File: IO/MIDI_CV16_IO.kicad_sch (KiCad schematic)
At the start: 111 parts, among them J1 Conn_01x10_Male, J10 AudioJack2_SwitchT, J11 Conn_01x10_Male, J12 AudioJack2_SwitchT, J13 AudioJack2_SwitchT, J14 AudioJack2_SwitchT, J15 AudioJack2_SwitchT, J16 AudioJack2_SwitchT, J17 AudioJack2_SwitchT, J18 AudioJack2_SwitchT, J19 AudioJack2_SwitchT, J2 Conn_01x10_Male, J20 Conn_01x10_Male, J3 AudioJack2_SwitchT, J4 AudioJack2_SwitchT, J5 AudioJack2_SwitchT, J6 AudioJack2_SwitchT, J7 AudioJack2_SwitchT, J8 AudioJack2_SwitchT, J9 AudioJack2_SwitchT, SW1 SW_SPST, SW2 SW_SPST, SW3 SW_SPST

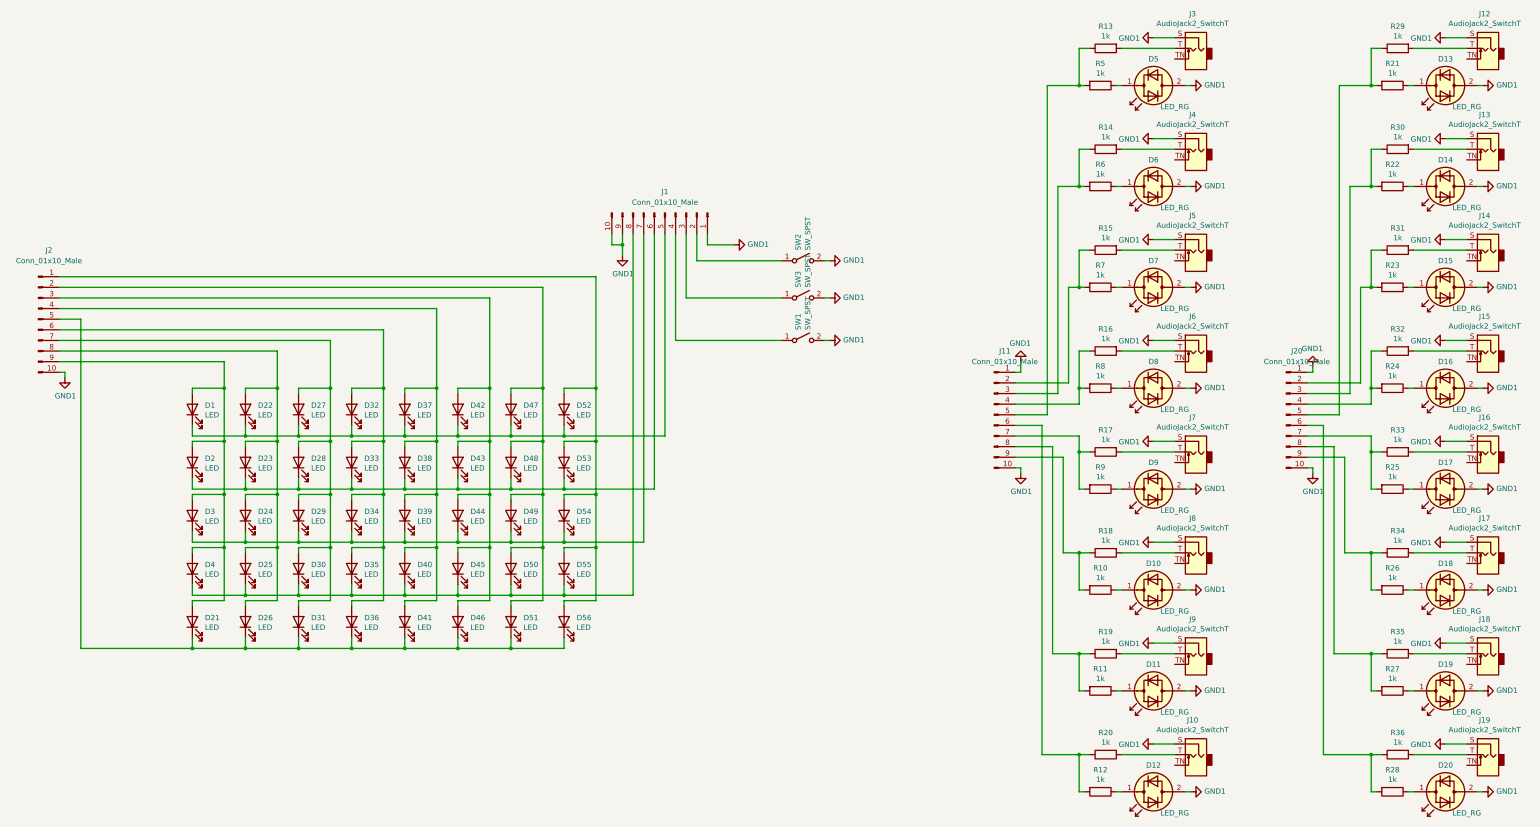
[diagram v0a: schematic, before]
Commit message: Update PCBs to V3.0
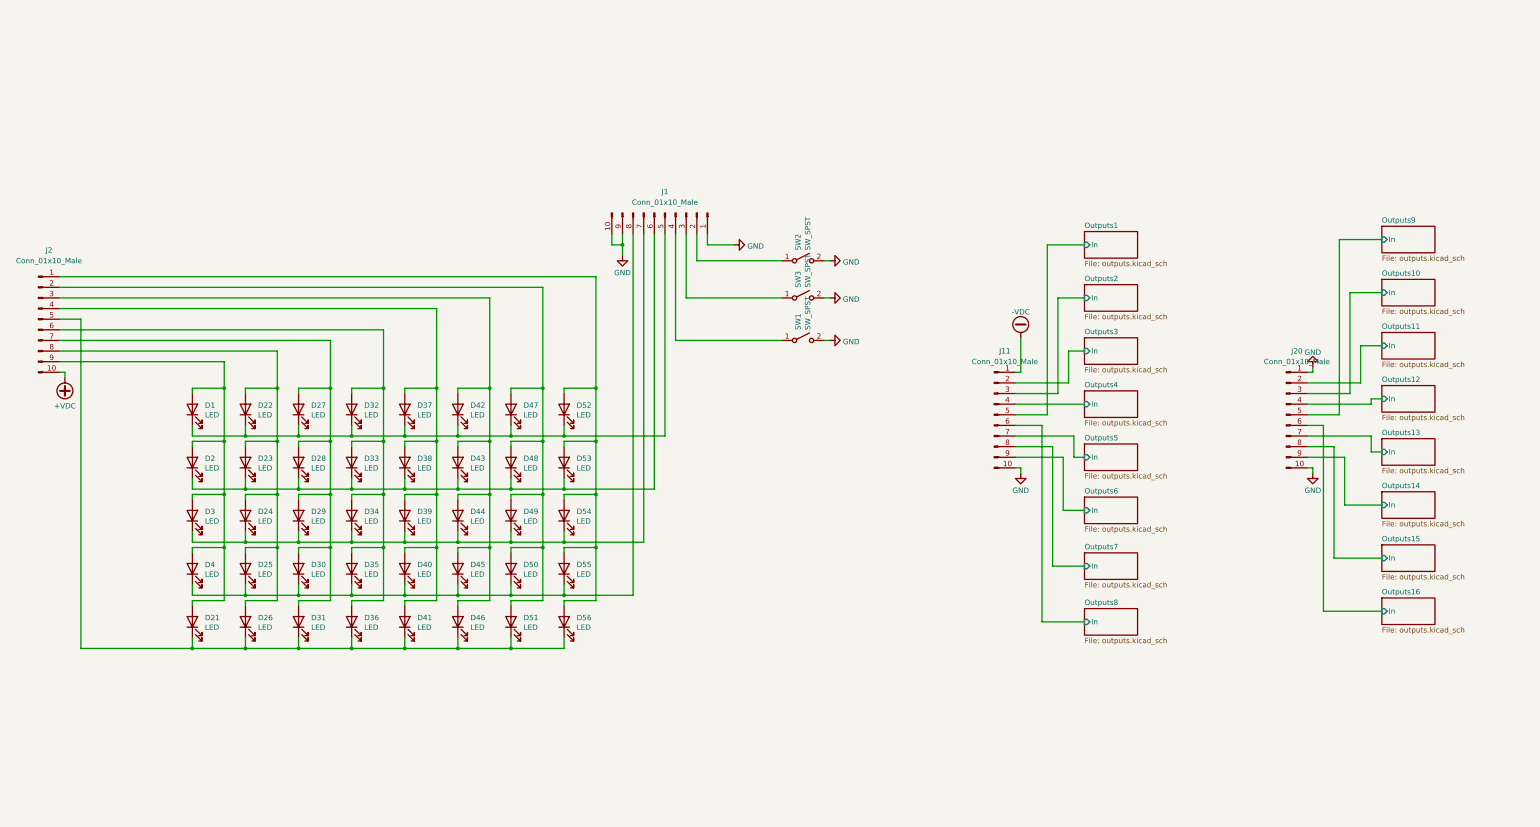
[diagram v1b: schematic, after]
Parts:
- removed D10, D11, D12, D13, D14, D15, D16, D17, D18, D19, D20, D5, D6, D7, D8, D9: LED_RG, LED_THT:LED_D5.0mm_FlatTop, symbol Device:LED_Dual_Bidirectional
- removed J10, J12, J13, J14, J15, J16, J17, J18, J19, J3, J4, J5, J6, J7, J8, J9: AudioJack2_SwitchT, Custom_FP:PJ398SM, symbol Connector_Audio:AudioJack2_SwitchT
- removed R10, R11, R12, R13, R14, R15, R16, R17, R18, R19, R20, R21, R22, R23, R24, R25, R26, R27, R28, R29, R30, R31, R32, R33, R34, R35, R36, R5, R6, R7, R8, R9: 1k, Resistor_SMD:R_0603_1608Metric, symbol Device:R
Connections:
- net Outputs3/In: now reaches J11.2 (Pin_2)
- net Outputs2/In: now reaches J11.3 (Pin_3)
- net Outputs4/In: now reaches J11.4 (Pin_4)
- net Outputs1/In: now reaches J11.5 (Pin_5)
- net Outputs8/In: now reaches J11.6 (Pin_6)
- net Outputs5/In: now reaches J11.7 (Pin_7)
- net Outputs7/In: now reaches J11.8 (Pin_8)
- net Outputs6/In: now reaches J11.9 (Pin_9)
- net Outputs11/In: now reaches J20.2 (Pin_2)
- net Outputs10/In: now reaches J20.3 (Pin_3)
- net Outputs12/In: now reaches J20.4 (Pin_4)
- net Outputs9/In: now reaches J20.5 (Pin_5)
- net Outputs16/In: now reaches J20.6 (Pin_6)
- net Outputs13/In: now reaches J20.7 (Pin_7)
- net Outputs15/In: now reaches J20.8 (Pin_8)
- net Outputs14/In: now reaches J20.9 (Pin_9)
- net GND1 renamed GND
- net GND: no longer J11.1 (Pin_1), J2.10 (Pin_10)
- new net +VDC: J2.10 (Pin_10)
- new net -VDC: J11.1 (Pin_1)
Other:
- added sheet Outputs1 (outputs.kicad_sch)
- added sheet Outputs10 (outputs.kicad_sch)
- added sheet Outputs11 (outputs.kicad_sch)
- added sheet Outputs12 (outputs.kicad_sch)
- added sheet Outputs13 (outputs.kicad_sch)
- added sheet Outputs14 (outputs.kicad_sch)
- added sheet Outputs15 (outputs.kicad_sch)
- added sheet Outputs16 (outputs.kicad_sch)
- added sheet Outputs2 (outputs.kicad_sch)
- added sheet Outputs3 (outputs.kicad_sch)
- added sheet Outputs4 (outputs.kicad_sch)
- added sheet Outputs5 (outputs.kicad_sch)
- added sheet Outputs6 (outputs.kicad_sch)
- added sheet Outputs7 (outputs.kicad_sch)
- added sheet Outputs8 (outputs.kicad_sch)
- added sheet Outputs9 (outputs.kicad_sch)

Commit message: Layout v3.1
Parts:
- J1, J11, J2, J20: footprint Connector_PinHeader_2.54mm:PinHeader_1x10_P2.54mm_Vertical_SMD_Pin1Left -> Connector_PinHeader_2.54mm:PinHeader_1x10_P2.54mm_Vertical_SMD_Pin1Right
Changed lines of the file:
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@@
       (effects (font (size 1.27 1.27)))
     )
-    (property "Footprint" "Connector_PinHeader_2.54mm:PinHeader_1x10_P2.54mm_Vertical_SMD_Pin1Left" (at 267.97 121.92 0)
+    (property "Footprint" "Connector_PinHeader_2.54mm:PinHeader_1x10_P2.54mm_Vertical_SMD_Pin1Right" (at 267.97 121.92 0)
       (effects (font (size 1.27 1.27)) hide)
     )
@@
       (effects (font (size 1.27 1.27)))
     )
-    (property "Footprint" "Connector_PinHeader_2.54mm:PinHeader_1x10_P2.54mm_Vertical_SMD_Pin1Left" (at 337.82 121.92 0)
+    (property "Footprint" "Connector_PinHeader_2.54mm:PinHeader_1x10_P2.54mm_Vertical_SMD_Pin1Right" (at 337.82 121.92 0)
       (effects (font (size 1.27 1.27)) hide)
     )
@@
       (effects (font (size 1.27 1.27)))
     )
-    (property "Footprint" "Connector_PinHeader_2.54mm:PinHeader_1x10_P2.54mm_Vertical_SMD_Pin1Left" (at 39.37 99.06 0)
+    (property "Footprint" "Connector_PinHeader_2.54mm:PinHeader_1x10_P2.54mm_Vertical_SMD_Pin1Right" (at 39.37 99.06 0)
       (effects (font (size 1.27 1.27)) hide)
     )
@@
       (effects (font (size 1.27 1.27)))
     )
-    (property "Footprint" "Connector_PinHeader_2.54mm:PinHeader_1x10_P2.54mm_Vertical_SMD_Pin1Left" (at 189.23 73.66 0)
-      (effects (font (size 1.27 1.27)) hide)
-    )
+    (property "Footprint" "Connector_PinHeader_2.54mm:PinHeader_1x10_P2.54mm_Vertical_SMD_Pin1Right" (at 189.23 73.66 0)
+      (effects (font (size 1.27 1.27)) hide)
+    )
